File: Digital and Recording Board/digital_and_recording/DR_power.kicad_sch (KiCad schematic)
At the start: 14 parts

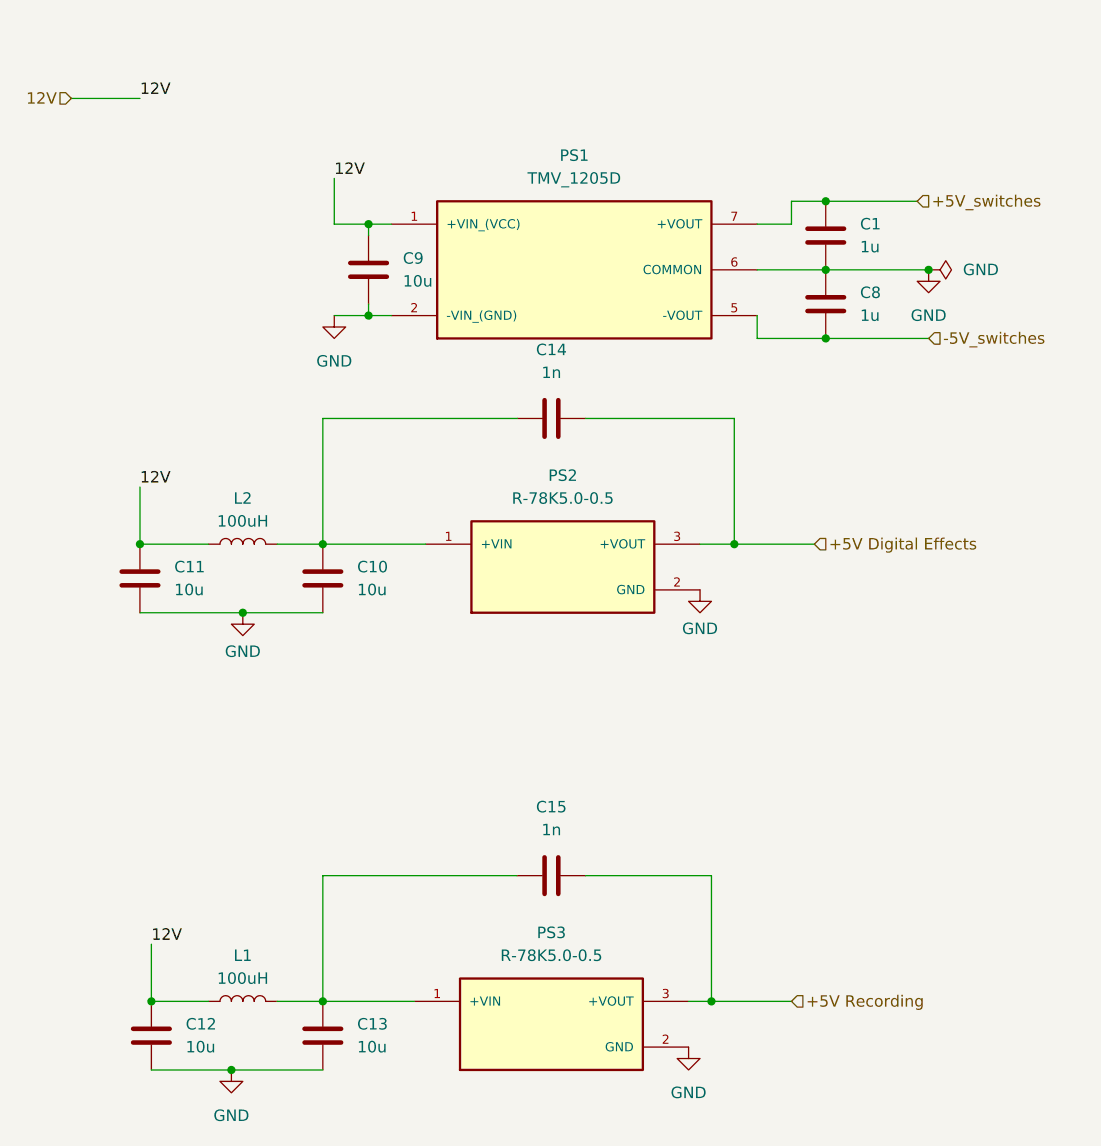
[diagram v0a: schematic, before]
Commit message: layout for digital board is essentially complete
current draw for the screen may fuck us if it is too high
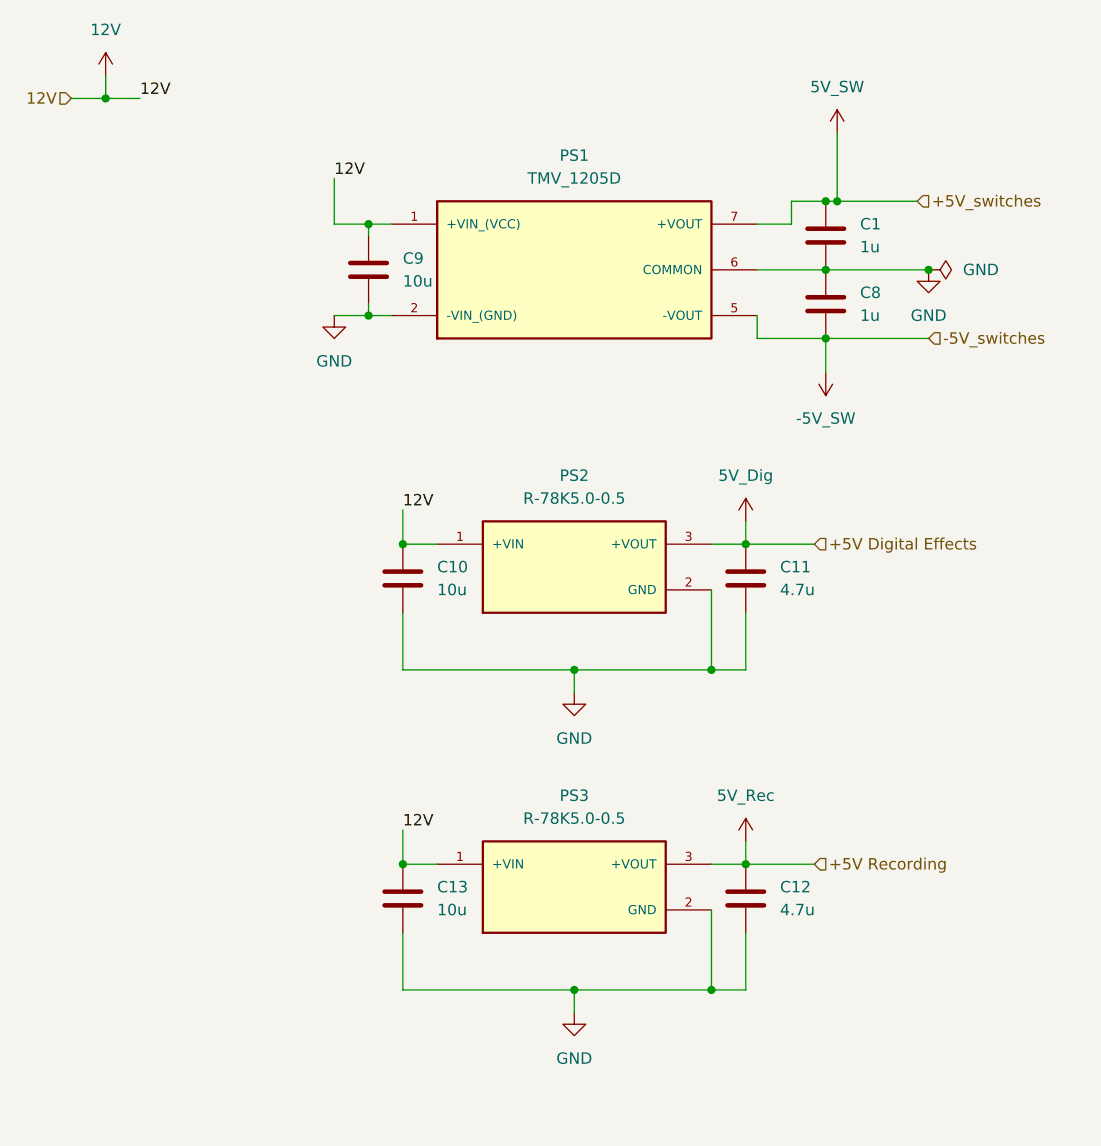
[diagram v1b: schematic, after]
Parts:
- removed C14, C15: 1n, Capacitor_SMD:C_0603_1608Metric, symbol Device:C
- removed L1, L2: 100uH, Inductor_SMD:L_0603_1608Metric, symbol Device:L
- C11, C12: value 10u -> 4.7u
- PS1: footprint TMV_1205D:CONV_TMV_1205D -> Kyle's Footprints:CONV_TMV_1205D
- PS2, PS3: footprint R-78K5.0-0.5:CONV_R-78K5.0-0.5 -> Kyle's Footprints:CONV_R-78K5.0-0.5
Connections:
- net 12V: now also C10.1, C13.1, PS2.1 (+VIN), PS3.1 (+VIN); no longer C11.1, C12.1
- net +5V Digital Effects renamed 5V_Dig
- net 5V_Dig: now also C11.1
- net +5V Recording renamed 5V_Rec
- net 5V_Rec: now also C12.1
- net +5V_switches renamed 5V_SW
- net -5V_switches renamed -5V_SW
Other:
- moved on the sheet: C12, C13, PS3
